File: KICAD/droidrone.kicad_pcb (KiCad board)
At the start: 2 copper layers, 50 x 50 mm, 52 parts, among them IC1 ATMEGA328PB, P1 USB_A, P2 CONN_01X06, P3 CONN_01X06, P4 CONN_01X02, P5 CONN_01X04, P6 CONN_01X06, P7 CONN_01X02, U1 TA4805S, U4 LP2950L-3.3V, Y1 Crystal

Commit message: size 100x50
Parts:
- moved P7 92.0 mm to (145.0, 50.0)
- moved D10 72.3 mm to (160.0, 65.0)
- moved D7 62.0 mm to (140.0, 65.0)
- moved D17 61.2 mm to (190.0, 65.0)
- moved D14 60.6 mm to (175.0, 65.0)
- moved 10k2 54.1 mm to (76.6, 116.8)
- moved 10k3 54.1 mm to (130.0, 115.4)
- moved 2.2k1 54.1 mm to (135.2, 115.4)
- moved 3.3k1 54.1 mm to (71.5, 116.8)
- moved 0.1uF5 54.1 mm to (84.0, 116.2)
- moved 22pF2 54.1 mm to (124.8, 115.9)
- moved P5 54.1 mm to (88.1, 103.7)
- moved 0.1uF2 54.1 mm to (94.8, 115.6)
- moved 0.1uF4 54.1 mm to (143.0, 104.3)
- moved 0.1uF6 54.1 mm to (156.1, 91.3)
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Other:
- board size 50 x 50 mm -> 100 x 50 mm

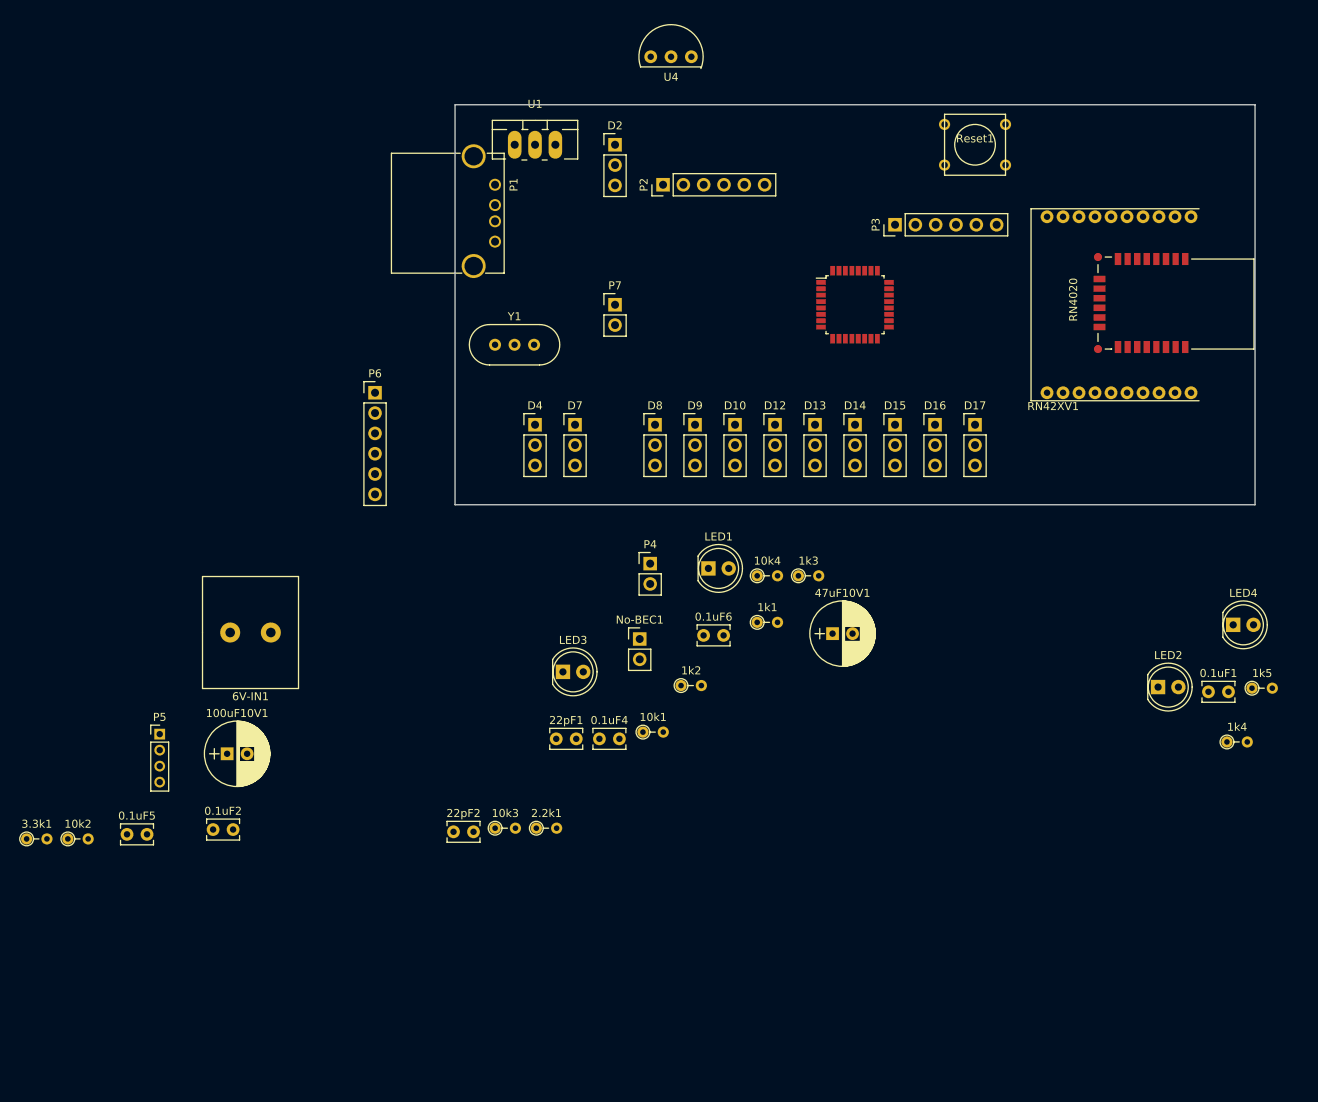
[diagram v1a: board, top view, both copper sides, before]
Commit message: add sub pcb
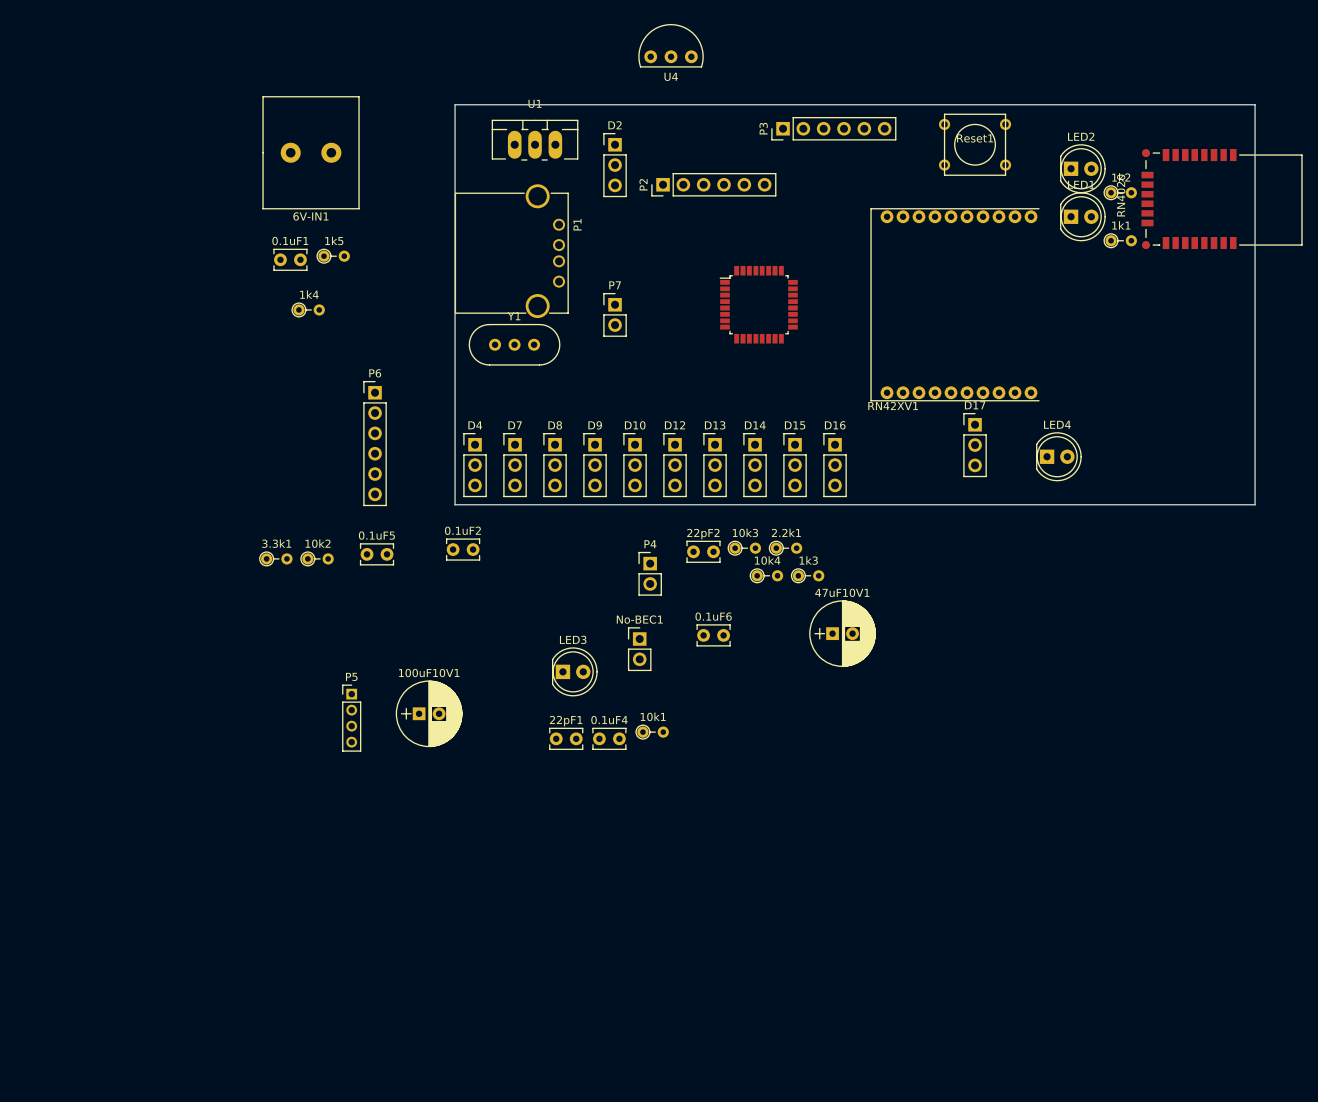
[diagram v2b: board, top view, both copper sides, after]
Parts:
- moved 1k4 128.0 mm to (105.5, 50.6)
- moved 1k5 128.0 mm to (108.6, 43.9)
- moved 0.1uF1 128.0 mm to (103.2, 44.4)
- moved 1k2 81.8 mm to (207.0, 36.0)
- moved LED2 65.7 mm to (202.0, 33.0)
- moved 1k1 65.1 mm to (207.0, 42.0)
- moved LED1 63.1 mm to (202.0, 39.0)
- moved 6V-IN1 60.4 mm to (107.0, 31.0)
- moved 22pF2 46.1 mm to (154.8, 80.9)
- moved 0.1uF2 46.1 mm to (124.8, 80.6)
- moved 0.1uF5 46.1 mm to (114.0, 81.2)
- moved 10k2 46.1 mm to (106.6, 81.8)
- moved 10k3 46.1 mm to (160.0, 80.4)
- moved 2.2k1 46.1 mm to (165.2, 80.4)
- moved 3.3k1 46.1 mm to (101.5, 81.8)
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
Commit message: same chg.
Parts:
- moved 100uF10V1 84.1 mm to (142.5, 20.0)
- moved 3.3k1 82.4 mm to (172.5, 40.0)
- moved 47uF10V1 81.4 mm to (132.5, 20.0)
- moved 10k2 76.7 mm to (172.5, 42.5)
- moved 0.1uF4 74.4 mm to (147.5, 30.0)
- moved 0.1uF6 61.3 mm to (155.0, 30.0)
- moved 0.1uF5 52.9 mm to (150.0, 42.5)
- moved LED3 49.5 mm to (120.0, 50.0)
- moved 1k3 49.1 mm to (172.5, 35.0)
- moved 22pF1 45.4 mm to (127.5, 60.0)
- moved 2.2k1 43.6 mm to (172.5, 37.5)
- moved No-BEC1 42.1 mm to (172.5, 57.5)
- moved D2 41.4 mm to (127.5, 67.5)
- moved 10k1 38.9 mm to (177.5, 77.5)
- moved 0.1uF2 38.7 mm to (157.5, 60.0)
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
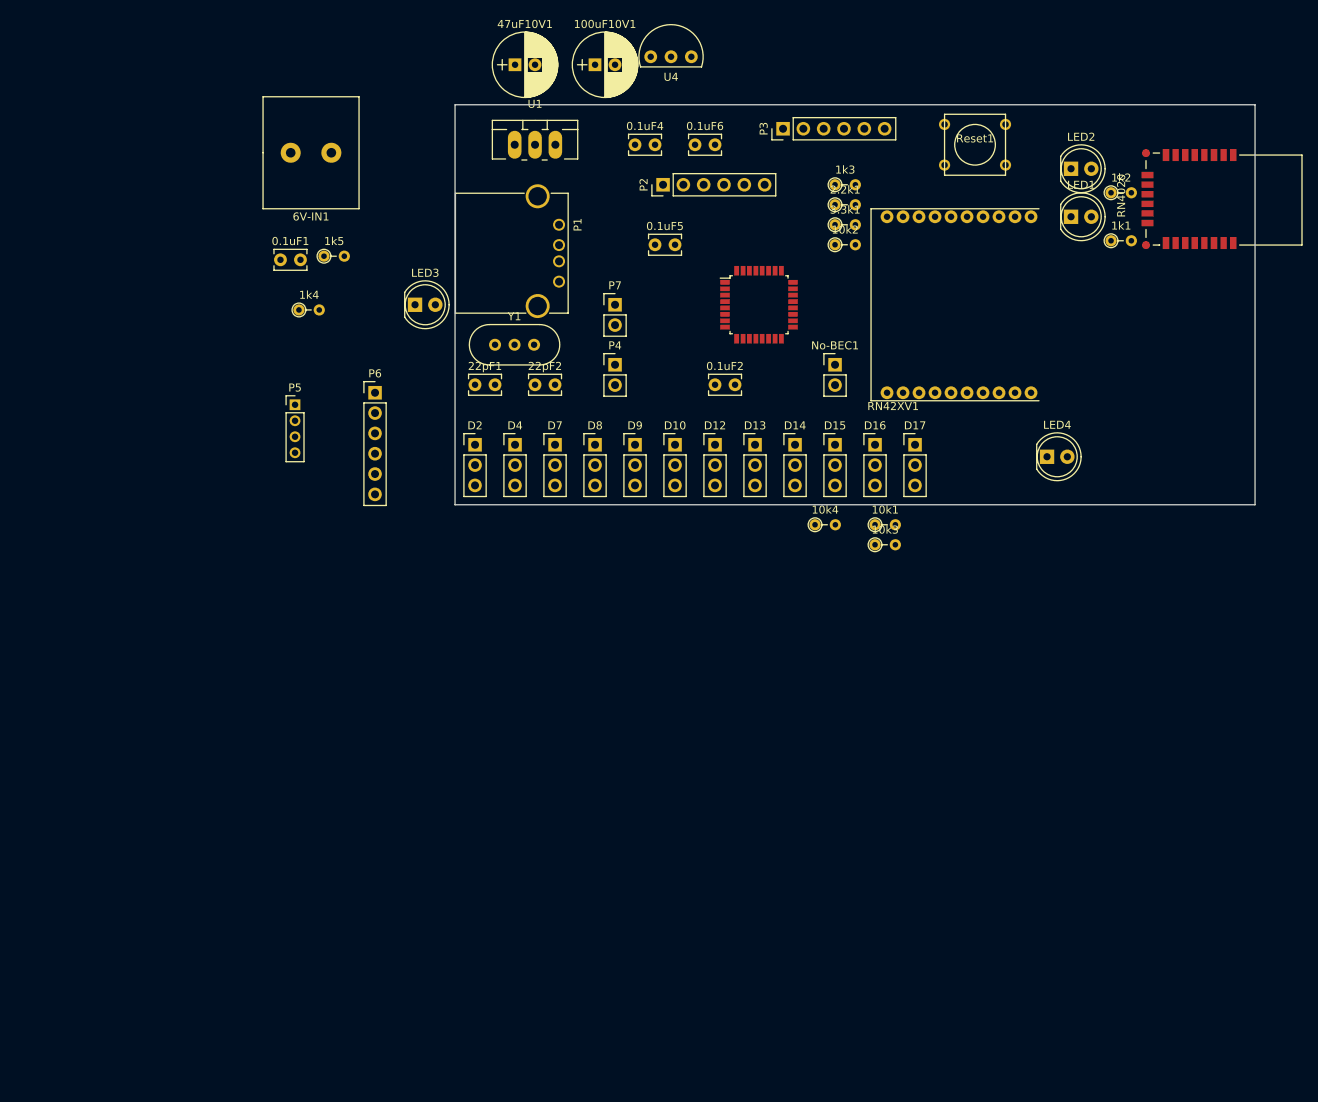
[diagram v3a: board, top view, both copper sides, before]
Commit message: add HC-06 BT mod
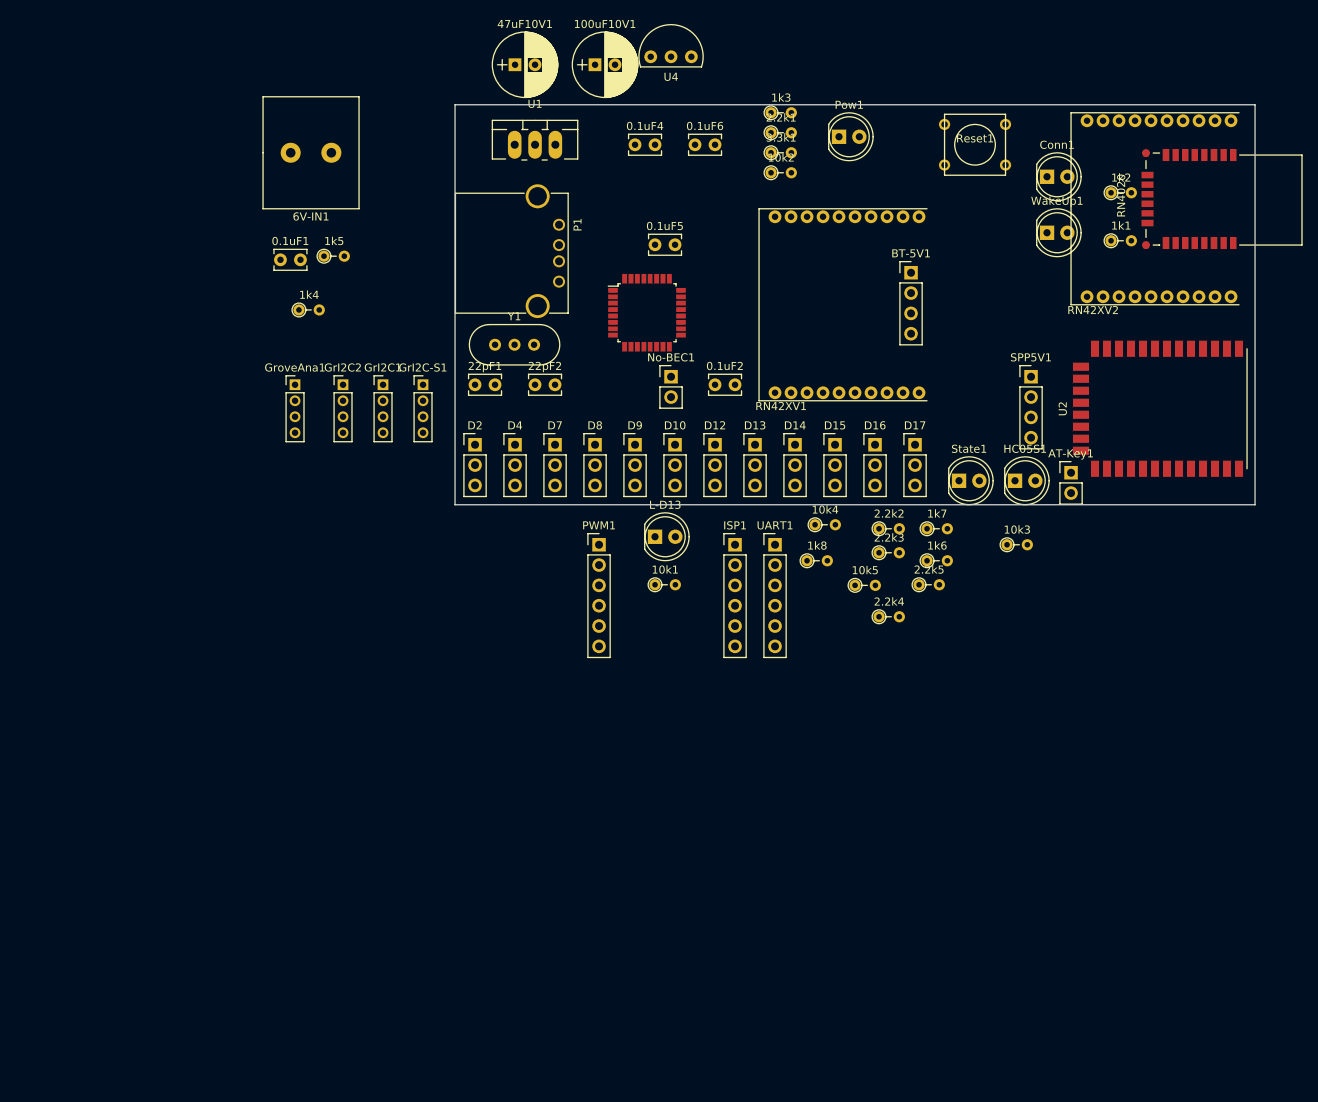
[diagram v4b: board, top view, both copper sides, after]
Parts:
- removed LED1, LED2, LED3, LED4: LED, LEDs:LED_D5.0mm
- removed P2, P3, P6: CONN_01X06, Pin_Headers:Pin_Header_Straight_1x06_Pitch2.54mm
- removed P4, P7: CONN_01X02, Pin_Headers:Pin_Header_Straight_1x02_Pitch2.54mm
- removed P5: CONN_01X04, Pin_Headers:Pin_Header_Straight_1x04_Pitch2.00mm
- added 10k5: 10k, Resistors_ThroughHole:R_Axial_DIN0204_L3.6mm_D1.6mm_P2.54mm_Vertical, F.Cu at (175.0, 85.1)
- added 1k6: 1k, Resistors_ThroughHole:R_Axial_DIN0204_L3.6mm_D1.6mm_P2.54mm_Vertical, F.Cu at (184.0, 82.0)
- added 1k7: 1k, Resistors_ThroughHole:R_Axial_DIN0204_L3.6mm_D1.6mm_P2.54mm_Vertical, F.Cu at (184.0, 78.0)
- added 1k8: 1k, Resistors_ThroughHole:R_Axial_DIN0204_L3.6mm_D1.6mm_P2.54mm_Vertical, F.Cu at (169.0, 82.0)
- added 2.2k2: 2.2k, Resistors_ThroughHole:R_Axial_DIN0204_L3.6mm_D1.6mm_P2.54mm_Vertical, F.Cu at (178.0, 78.0)
- added 2.2k3: 2.2k, Resistors_ThroughHole:R_Axial_DIN0204_L3.6mm_D1.6mm_P2.54mm_Vertical, F.Cu at (178.0, 81.0)
- added 2.2k4: 2.2k, Resistors_ThroughHole:R_Axial_DIN0204_L3.6mm_D1.6mm_P2.54mm_Vertical, F.Cu at (178.0, 89.0)
- added 2.2k5: 2.2k, Resistors_ThroughHole:R_Axial_DIN0204_L3.6mm_D1.6mm_P2.54mm_Vertical, F.Cu at (183.0, 85.0)
- added AT-Key1: JUMPER, Pin_Headers:Pin_Header_Straight_1x02_Pitch2.54mm, F.Cu at (202.0, 71.0)
- added BT-5V1: CONN_01X04, Pin_Headers:Pin_Header_Straight_1x04_Pitch2.54mm, F.Cu at (182.0, 46.0)
- added Conn1: LED, LEDs:LED_D5.0mm, F.Cu at (199.0, 34.0)
- added GrI2C-S1: CONN_01X04, Pin_Headers:Pin_Header_Straight_1x04_Pitch2.00mm, F.Cu at (121.0, 60.0)
- added GrI2C1: CONN_01X04, Pin_Headers:Pin_Header_Straight_1x04_Pitch2.00mm, F.Cu at (116.0, 60.0)
- added GrI2C2: CONN_01X04, Pin_Headers:Pin_Header_Straight_1x04_Pitch2.00mm, F.Cu at (111.0, 60.0)
- added GroveAna1: CONN_01X04, Pin_Headers:Pin_Header_Straight_1x04_Pitch2.00mm, F.Cu at (105.0, 60.0)
- added HC05S1: LED, LEDs:LED_D5.0mm, F.Cu at (195.0, 72.0)
- added ISP1: CONN_01X06, Pin_Headers:Pin_Header_Straight_1x06_Pitch2.54mm, F.Cu at (160.0, 80.0)
- added L-D13: LED, LEDs:LED_D5.0mm, F.Cu at (150.0, 79.0)
- added PWM1: CONN_01X06, Pin_Headers:Pin_Header_Straight_1x06_Pitch2.54mm, F.Cu at (143.0, 80.0)
- added Pow1: LED, LEDs:LED_D5.0mm, F.Cu at (173.0, 29.0)
- added RN42XV2: RN42XV, lib:RN42XV, F.Cu at (220.0, 38.0)
- added SPP5V1: CONN_01X04, Pin_Headers:Pin_Header_Straight_1x04_Pitch2.54mm, F.Cu at (197.0, 59.0)
- added State1: LED, LEDs:LED_D5.0mm, F.Cu at (188.0, 72.0)
- added U2: ITEAD_HC-05, lib:HC-05-06, F.Cu at (205.0, 63.0)
- added UART1: CONN_01X06, Pin_Headers:Pin_Header_Straight_1x06_Pitch2.54mm, F.Cu at (165.0, 80.0)
- added WakeUp1: LED, LEDs:LED_D5.0mm, F.Cu at (199.0, 41.0)
- moved 10k1 28.5 mm to (150.0, 85.0)
- moved No-BEC1 20.6 mm to (152.0, 59.0)
- moved 10k3 16.5 mm to (194.0, 80.0)
- moved IC1 14.0 mm to (149.0, 51.0)
- moved RN42XV1 14.0 mm to (181.0, 50.0)
- moved 10k2 12.0 mm to (164.5, 33.5)
- moved 1k3 12.0 mm to (164.5, 26.0)
- moved 2.2k1 12.0 mm to (164.5, 28.5)
- moved 3.3k1 12.0 mm to (164.5, 31.0)
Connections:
- 10k2 pad 1: Net-(0.1uF5-Pad2) -> +5V
- 10k2 pad 2: +5V -> Net-(0.1uF5-Pad2)
- P1 pad 2: Net-(P1-Pad2) -> (no net)
- P1 pad 3: Net-(P1-Pad3) -> (no net)
- RN4020 pad 1: GND -> Net-(Conn1-Pad1)
- RN4020 pad 11: Net-(RN4020-Pad11) -> (no net)
- RN4020 pad 13: Net-(RN4020-Pad13) -> (no net)
- RN4020 pad 14: Net-(RN4020-Pad14) -> (no net)
- RN4020 pad 15: +3V3 -> Net-(RN4020-Pad15)
- RN4020 pad 16: GND -> Net-(Conn1-Pad1)
- RN4020 pad 17: Net-(RN4020-Pad17) -> (no net)
- RN4020 pad 18: Net-(RN4020-Pad18) -> (no net)
- RN4020 pad 19: Net-(RN4020-Pad19) -> (no net)
- RN4020 pad 2: Net-(RN4020-Pad2) -> (no net)
- RN4020 pad 20: Net-(RN4020-Pad20) -> (no net)
- RN4020 pad 21: Net-(RN4020-Pad21) -> (no net)
- RN4020 pad 22: Net-(RN4020-Pad22) -> (no net)
- RN4020 pad 23: +3V3 -> Net-(RN4020-Pad15)
- RN4020 pad 24: GND -> Net-(Conn1-Pad1)
- RN4020 pad 3: Net-(RN4020-Pad3) -> (no net)
- RN4020 pad 4: Net-(RN4020-Pad4) -> (no net)
- RN4020 pad 5: Net-(1k3-Pad2) -> Net-(RN4020-Pad5)
- RN4020 pad 6: Net-(2.2k1-Pad2) -> Net-(RN4020-Pad6)
- RN4020 pad 7: +3V3 -> Net-(RN4020-Pad15)
- RN4020 pad 8: GND -> Net-(Conn1-Pad1)
- RN4020 pad 9: GND -> Net-(Conn1-Pad1)
- RN42XV1 pad 11: Net-(RN42XV1-Pad11) -> (no net)
- RN42XV1 pad 13: Net-(RN42XV1-Pad13) -> (no net)
- RN42XV1 pad 14: Net-(RN42XV1-Pad14) -> (no net)
- RN42XV1 pad 15: Net-(RN42XV1-Pad15) -> (no net)
- RN42XV1 pad 17: Net-(RN42XV1-Pad17) -> (no net)
- RN42XV1 pad 18: Net-(RN42XV1-Pad18) -> (no net)
- RN42XV1 pad 19: Net-(RN42XV1-Pad19) -> (no net)
- RN42XV1 pad 20: Net-(RN42XV1-Pad20) -> (no net)
- RN42XV1 pad 4: Net-(RN42XV1-Pad4) -> (no net)
- RN42XV1 pad 5: Net-(RN42XV1-Pad5) -> (no net)
- RN42XV1 pad 6: Net-(RN42XV1-Pad6) -> (no net)
- RN42XV1 pad 7: Net-(RN42XV1-Pad7) -> (no net)
- RN42XV1 pad 8: Net-(RN42XV1-Pad8) -> (no net)
- RN42XV1 pad 9: Net-(RN42XV1-Pad9) -> (no net)

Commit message: chg sch
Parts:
- moved D4 41.0 mm to (157.5, 35.0)
- moved D2 36.9 mm to (145.0, 35.0)
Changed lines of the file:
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@@
-(kicad_pcb (version 4) (host pcbnew 4.0.2-stable)
+(kicad_pcb (version 4) (host pcbnew 4.0.1-stable)
   (general
     (links 175)
     (no_connects 175)
-    (area 124.924999 24.924999 225.075001 75.075001)
+    (area 90.000001 13.815 243 96.065)
     (thickness 1.6)
     (drawings 10)
@@
   )
   (module Pin_Headers:Pin_Header_Straight_1x03_Pitch2.54mm (layer F.Cu)
-    (at 127.5 67.5)
+    (at 145 35)
     (descr "Through hole straight pin header, 1x03, 2.54mm pitch, single row")
     (tags "Through hole pin header THT 1x03 2.54mm single row")
@@
   )
   (module Pin_Headers:Pin_Header_Straight_1x03_Pitch2.54mm (layer F.Cu)
-    (at 132.5 67.5)
+    (at 157.5 35)
     (descr "Through hole straight pin header, 1x03, 2.54mm pitch, single row")
     (tags "Through hole pin header THT 1x03 2.54mm single row")
